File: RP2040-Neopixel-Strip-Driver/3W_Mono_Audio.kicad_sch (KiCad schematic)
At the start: 0 parts

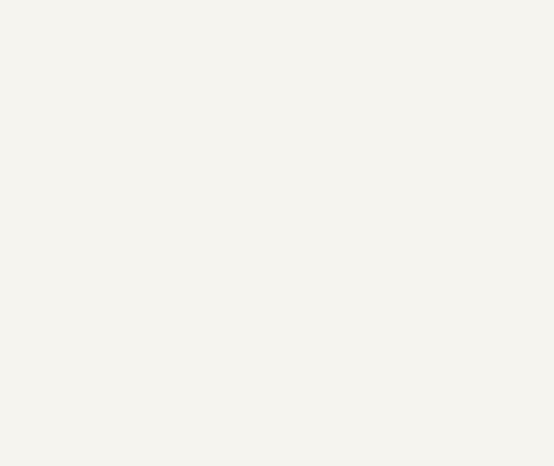
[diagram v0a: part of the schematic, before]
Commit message: Created symbol for Audio Amp, associated footprint and model from KiCad library
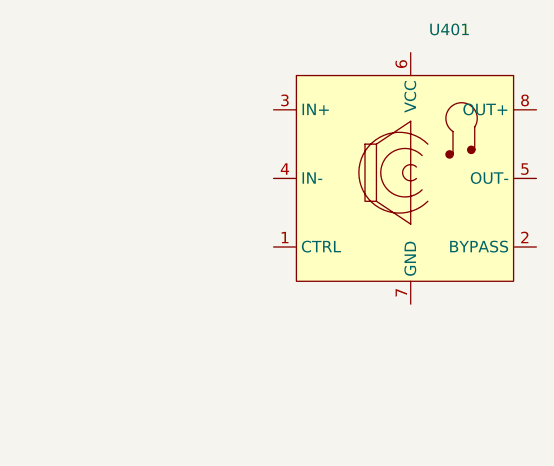
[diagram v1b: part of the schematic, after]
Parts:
- added U401: (no value), symbol BreadstickLibrary:NS4150B
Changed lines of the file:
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@@
     (effects (font (size 1.27 1.27)) (justify left bottom))
   )
+  (symbol (lib_id "BreadstickLibrary:NS4150B") (at 149.86 106.68 0) (unit 1)
+    (in_bom yes) (on_board yes) (fields_autoplaced)
+    (property "Reference" "U401" (id 0) (at 151.8794 90.17 0)
+      (effects (font (size 1.27 1.27)) (justify left))
+    )
+    (property "Value" "" (id 1) (at 151.8794 92.71 0)
+      (effects (font (size 1.27 1.27)) (justify left))
+    )
+    (property "Footprint" "" (id 2) (at 185.42 67.31 0)
+      (effects (font (size 1.27 1.27)) hide)
+    )
+    (property "Datasheet" "" (id 3) (at 185.42 67.31 0)
+      (effects (font (size 1.27 1.27)) hide)
+    )
+    (property "JLCPCB P/N" "C189961" (id 4) (at 149.86 106.68 0)
+      (effects (font (size 1.27 1.27)) hide)
+    )
+    (pin "1")
+    (pin "2")
+    (pin "3")
+    (pin "4")
+    (pin "5")
+    (pin "6")
+    (pin "7")
+    (pin "8")
+  )
 )

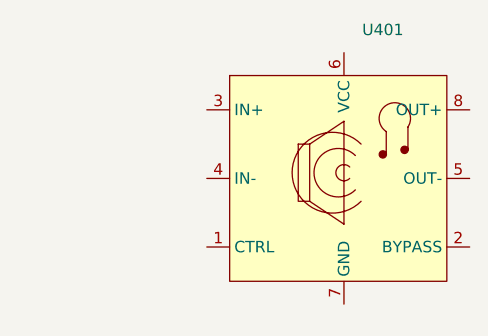
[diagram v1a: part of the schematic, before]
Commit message: Updated all IC symbols to have filled background, personal preference.
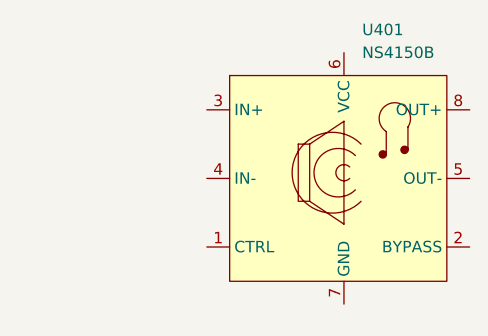
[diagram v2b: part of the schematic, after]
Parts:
- U401: value (none) -> NS4150B; footprint (none) -> Package_SO:MSOP-8-1EP_3x3mm_P0.65mm_EP1.73x1.85mm_ThermalVias
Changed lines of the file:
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@@
       (effects (font (size 1.27 1.27)) (justify left))
     )
-    (property "Value" "" (id 1) (at 151.8794 92.71 0)
+    (property "Value" "NS4150B" (id 1) (at 151.8794 92.71 0)
       (effects (font (size 1.27 1.27)) (justify left))
     )
-    (property "Footprint" "" (id 2) (at 185.42 67.31 0)
+    (property "Footprint" "Package_SO:MSOP-8-1EP_3x3mm_P0.65mm_EP1.73x1.85mm_ThermalVias" (id 2) (at 185.42 67.31 0)
       (effects (font (size 1.27 1.27)) hide)
     )
